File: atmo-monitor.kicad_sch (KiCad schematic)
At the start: 27 parts, among them J1 E-Ink, J2 Power, J3 Qwiic, J4 PM Sensor, SW1 Reset, SW2 1825232-1, U1 STM32F103CBT6, U2 LP2950-3.3_TO252

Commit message: Finished initial design
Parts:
- added Q1: IRLML0100TRPbF, Package_TO_SOT_SMD:SOT-23, symbol Transistor_FET:IRLML0030
- renumbered J2 to U3
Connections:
- net +3.3V: now also Q1.1 (G)
- net ENABLE: now also SW2.1 (B)
- net LBO: now also Q1.3 (D); no longer SW2.1 (B)
- net MCU-LBO: now reaches U1.10 (PA0)
- net MCU-LBO: now also Q1.2 (S)
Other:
- note added: "5V & Battery Power"
- note added: "Level Translation"
- moved on the sheet: H1, H2, H3, H4, J3, U3

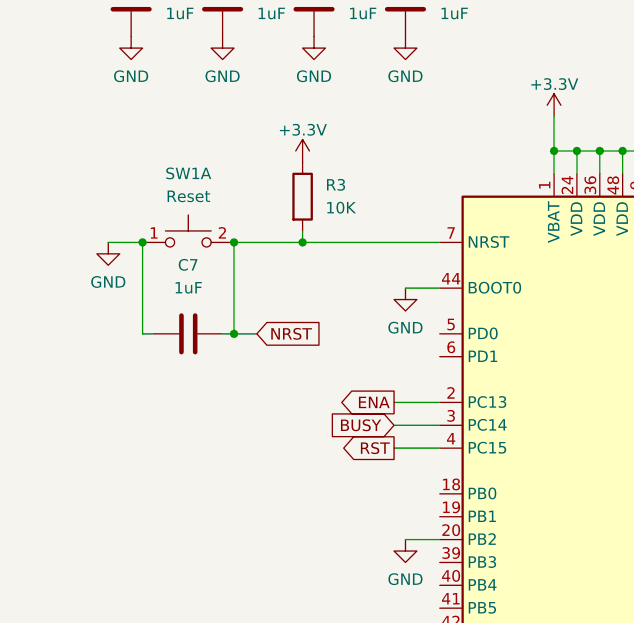
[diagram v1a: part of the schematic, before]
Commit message: Moved 2 signals from output limited ports
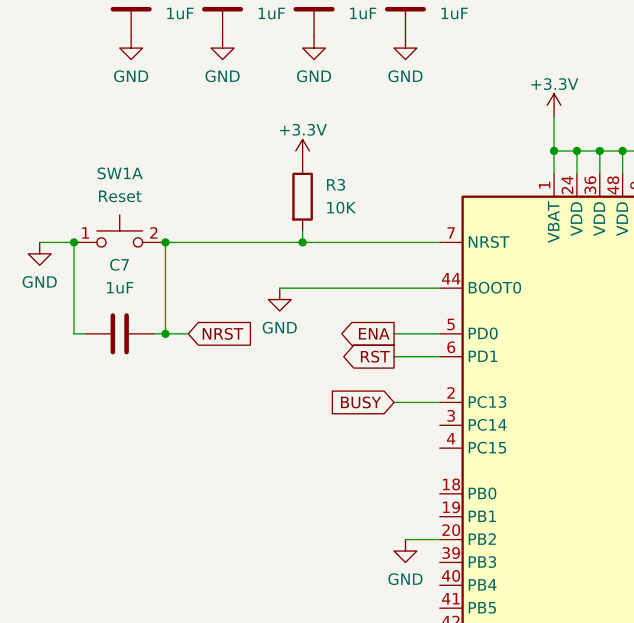
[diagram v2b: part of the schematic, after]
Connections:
- net BUSY: now also U1.2 (PC13); no longer U1.3 (PC14)
- net ENA: now also U1.5 (PD0); no longer U1.2 (PC13)
- net RST: now also U1.6 (PD1); no longer U1.4 (PC15)
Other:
- moved on the sheet: C7, SW1A
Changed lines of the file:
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@@
 	)
 	(junction
-		(at 45.72 57.15)
-		(diameter 0)
-		(color 0 0 0 0)
-	)
-	(junction
 		(at 204.47 30.48)
 		(diameter 0)
@@
 	)
 	(junction
-		(at 45.72 67.31)
+		(at 38.1 67.31)
 		(diameter 0)
 		(color 0 0 0 0)
@@
 	)
 	(junction
+		(at 38.1 57.15)
+		(diameter 0)
+		(color 0 0 0 0)
+	)
+	(junction
 		(at 165.1 50.8)
 		(diameter 0)
@@
 	)
 	(junction
-		(at 35.56 57.15)
+		(at 27.94 57.15)
 		(diameter 0)
 		(color 0 0 0 0)
@@
 	(wire
 		(pts
-			(xy 63.5 80.01) (xy 68.58 80.01)
+			(xy 63.5 69.85) (xy 68.58 69.85)
 		)
 		(stroke
@@
 	(wire
 		(pts
-			(xy 104.14 64.77) (xy 109.22 64.77)
+			(xy 38.1 57.15) (xy 53.34 57.15)
 		)
 		(stroke
@@
 	(wire
 		(pts
-			(xy 45.72 67.31) (xy 44.45 67.31)
+			(xy 104.14 64.77) (xy 109.22 64.77)
 		)
 		(stroke
@@
 	(wire
 		(pts
-			(xy 45.72 67.31) (xy 48.26 67.31)
+			(xy 38.1 67.31) (xy 36.83 67.31)
 		)
 		(stroke
@@
 	(wire
 		(pts
-			(xy 165.1 50.8) (xy 170.18 50.8)
+			(xy 38.1 67.31) (xy 40.64 67.31)
 		)
 		(stroke
@@
 	(wire
 		(pts
-			(xy 91.44 49.53) (xy 91.44 46.99)
+			(xy 165.1 50.8) (xy 170.18 50.8)
 		)
 		(stroke
@@
 	(wire
 		(pts
-			(xy 45.72 57.15) (xy 53.34 57.15)
+			(xy 91.44 49.53) (xy 91.44 46.99)
 		)
 		(stroke
@@
 	(wire
 		(pts
-			(xy 36.83 67.31) (xy 35.56 67.31)
+			(xy 29.21 67.31) (xy 27.94 67.31)
 		)
 		(stroke
@@
 	(wire
 		(pts
-			(xy 64.77 62.23) (xy 68.58 62.23)
+			(xy 176.53 39.37) (xy 176.53 41.91)
 		)
 		(stroke
@@
 	(wire
 		(pts
-			(xy 176.53 39.37) (xy 176.53 41.91)
+			(xy 171.45 101.6) (xy 179.07 101.6)
 		)
 		(stroke
@@
 	(wire
 		(pts
-			(xy 171.45 101.6) (xy 179.07 101.6)
+			(xy 173.99 34.29) (xy 173.99 36.83)
 		)
 		(stroke
@@
 	(wire
 		(pts
-			(xy 173.99 34.29) (xy 173.99 36.83)
+			(xy 119.38 177.8) (xy 110.49 177.8)
 		)
 		(stroke
@@
 	(wire
 		(pts
-			(xy 119.38 177.8) (xy 110.49 177.8)
+			(xy 173.99 36.83) (xy 176.53 36.83)
 		)
 		(stroke
@@
 	(wire
 		(pts
-			(xy 173.99 36.83) (xy 176.53 36.83)
+			(xy 50.8 62.23) (xy 68.58 62.23)
 		)
 		(stroke
@@
 	(wire
 		(pts
-			(xy 31.75 57.15) (xy 35.56 57.15)
+			(xy 24.13 57.15) (xy 27.94 57.15)
 		)
 		(stroke
@@
 	(wire
 		(pts
-			(xy 63.5 77.47) (xy 68.58 77.47)
+			(xy 63.5 67.31) (xy 68.58 67.31)
 		)
 		(stroke
@@
 	(wire
 		(pts
-			(xy 45.72 57.15) (xy 45.72 67.31)
+			(xy 38.1 57.15) (xy 38.1 67.31)
 		)
 		(stroke
@@
 	(wire
 		(pts
-			(xy 35.56 67.31) (xy 35.56 57.15)
+			(xy 27.94 67.31) (xy 27.94 57.15)
 		)
 		(stroke
@@
 	(global_label "RST"
 		(shape output)
-		(at 63.5 80.01 180)
+		(at 63.5 69.85 180)
 		(fields_autoplaced yes)
 		(effects
@@
 		)
 		(property "Intersheetrefs" "${INTERSHEET_REFS}"
-			(at 57.0677 80.01 0)
+			(at 57.0677 69.85 0)
 			(effects
 				(font
@@
 	(global_label "NRST"
 		(shape input)
-		(at 48.26 67.31 0)
+		(at 40.64 67.31 0)
 		(fields_autoplaced yes)
 		(effects
@@
 		)
 		(property "Intersheetrefs" "${INTERSHEET_REFS}"
-			(at 56.0228 67.31 0)
+			(at 48.4028 67.31 0)
 			(effects
 				(font
@@
 	(global_label "BUSY"
 		(shape input)
-		(at 63.5 77.47 180)
+		(at 63.5 74.93 180)
 		(fields_autoplaced yes)
 		(effects
@@
 		)
 		(property "Intersheetrefs" "${INTERSHEET_REFS}"
-			(at 55.6162 77.47 0)
+			(at 55.6162 74.93 0)
 			(effects
 				(font
@@
 	(global_label "ENA"
 		(shape output)
-		(at 63.5 74.93 180)
+		(at 63.5 67.31 180)
 		(fields_autoplaced yes)
 		(effects
@@
 		)
 		(property "Intersheetrefs" "${INTERSHEET_REFS}"
-			(at 56.9467 74.93 0)
+			(at 56.9467 67.31 0)
 			(effects
 				(font
@@
 	(symbol
 		(lib_id "Device:C")
-		(at 40.64 67.31 270)
+		(at 33.02 67.31 270)
 		(unit 1)
 		(exclude_from_sim no)
@@
 		(fields_autoplaced yes)
 		(property "Reference" "C7"
-			(at 40.64 59.69 90)
+			(at 33.02 59.69 90)
 			(effects
 				(font
@@
 		)
 		(property "Value" "1uF"
-			(at 40.64 62.23 90)
+			(at 33.02 62.23 90)
 			(effects
 				(font
@@
 		)
 		(property "Footprint" "Capacitor_SMD:C_1206_3216Metric_Pad1.33x1.80mm_HandSolder"
-			(at 36.83 68.2752 0)
+			(at 29.21 68.2752 0)
 			(effects
 				(font
@@
 		)
 		(property "Datasheet" "~"
-			(at 40.64 67.31 0)
+			(at 33.02 67.31 0)
 			(effects
 				(font
@@
 		)
 		(property "Description" "Unpolarized capacitor"
-			(at 40.64 67.31 0)
+			(at 33.02 67.31 0)
 			(effects
 				(font
@@
 	(symbol
 		(lib_id "Switch:SW_Push_Dual_x2")
-		(at 40.64 57.15 0)
+		(at 33.02 57.15 0)
 		(unit 1)
 		(exclude_from_sim no)
@@
 		(fields_autoplaced yes)
 		(property "Reference" "SW1"
-			(at 40.64 49.53 0)
+			(at 33.02 49.53 0)
 			(effects
 				(font
@@
 		)
 		(property "Value" "Reset"
-			(at 40.64 52.07 0)
+			(at 33.02 52.07 0)
 			(effects
 				(font
@@
 		)
 		(property "Footprint" "custom_footprint:OnShine KPT-1187B"
-			(at 40.64 52.07 0)
+			(at 33.02 52.07 0)
 			(effects
 				(font
@@
 		)
 		(property "Datasheet" "~"
-			(at 40.64 52.07 0)
+			(at 33.02 52.07 0)
 			(effects
 				(font
@@
 		)
 		(property "Description" "Push button switch, generic, separate symbols, four pins"
-			(at 40.64 57.15 0)
+			(at 33.02 57.15 0)
 			(effects
 				(font
@@
 	(symbol
 		(lib_id "power:GND")
-		(at 64.77 62.23 0)
+		(at 50.8 62.23 0)
 		(unit 1)
 		(exclude_from_sim no)
@@
 		(fields_autoplaced yes)
 		(property "Reference" "#PWR021"
-			(at 64.77 68.58 0)
+			(at 50.8 68.58 0)
 			(effects
 				(font
@@
 		)
 		(property "Value" "GND"
-			(at 64.77 66.6734 0)
+			(at 50.8 66.6734 0)
 			(effects
 				(font
@@
 		)
 		(property "Footprint" ""
-			(at 64.77 62.23 0)
+			(at 50.8 62.23 0)
 			(effects
 				(font
@@
 		)
 		(property "Datasheet" ""
-			(at 64.77 62.23 0)
+			(at 50.8 62.23 0)
 			(effects
 				(font
@@
 		)
 		(property "Description" ""
-			(at 64.77 62.23 0)
+			(at 50.8 62.23 0)
 			(effects
 				(font
@@
 	(symbol
 		(lib_id "power:GND")
-		(at 31.75 57.15 0)
+		(at 24.13 57.15 0)
 		(unit 1)
 		(exclude_from_sim no)
@@
 		(fields_autoplaced yes)
 		(property "Reference" "#PWR022"
-			(at 31.75 63.5 0)
+			(at 24.13 63.5 0)
 			(effects
 				(font
@@
 		)
 		(property "Value" "GND"
-			(at 31.75 61.5934 0)
+			(at 24.13 61.5934 0)
 			(effects
 				(font
@@
 		)
 		(property "Footprint" ""
-			(at 31.75 57.15 0)
+			(at 24.13 57.15 0)
 			(effects
 				(font
@@
 		)
 		(property "Datasheet" ""
-			(at 31.75 57.15 0)
+			(at 24.13 57.15 0)
 			(effects
 				(font
@@
 		)
 		(property "Description" ""
-			(at 31.75 57.15 0)
+			(at 24.13 57.15 0)
 			(effects
 				(font

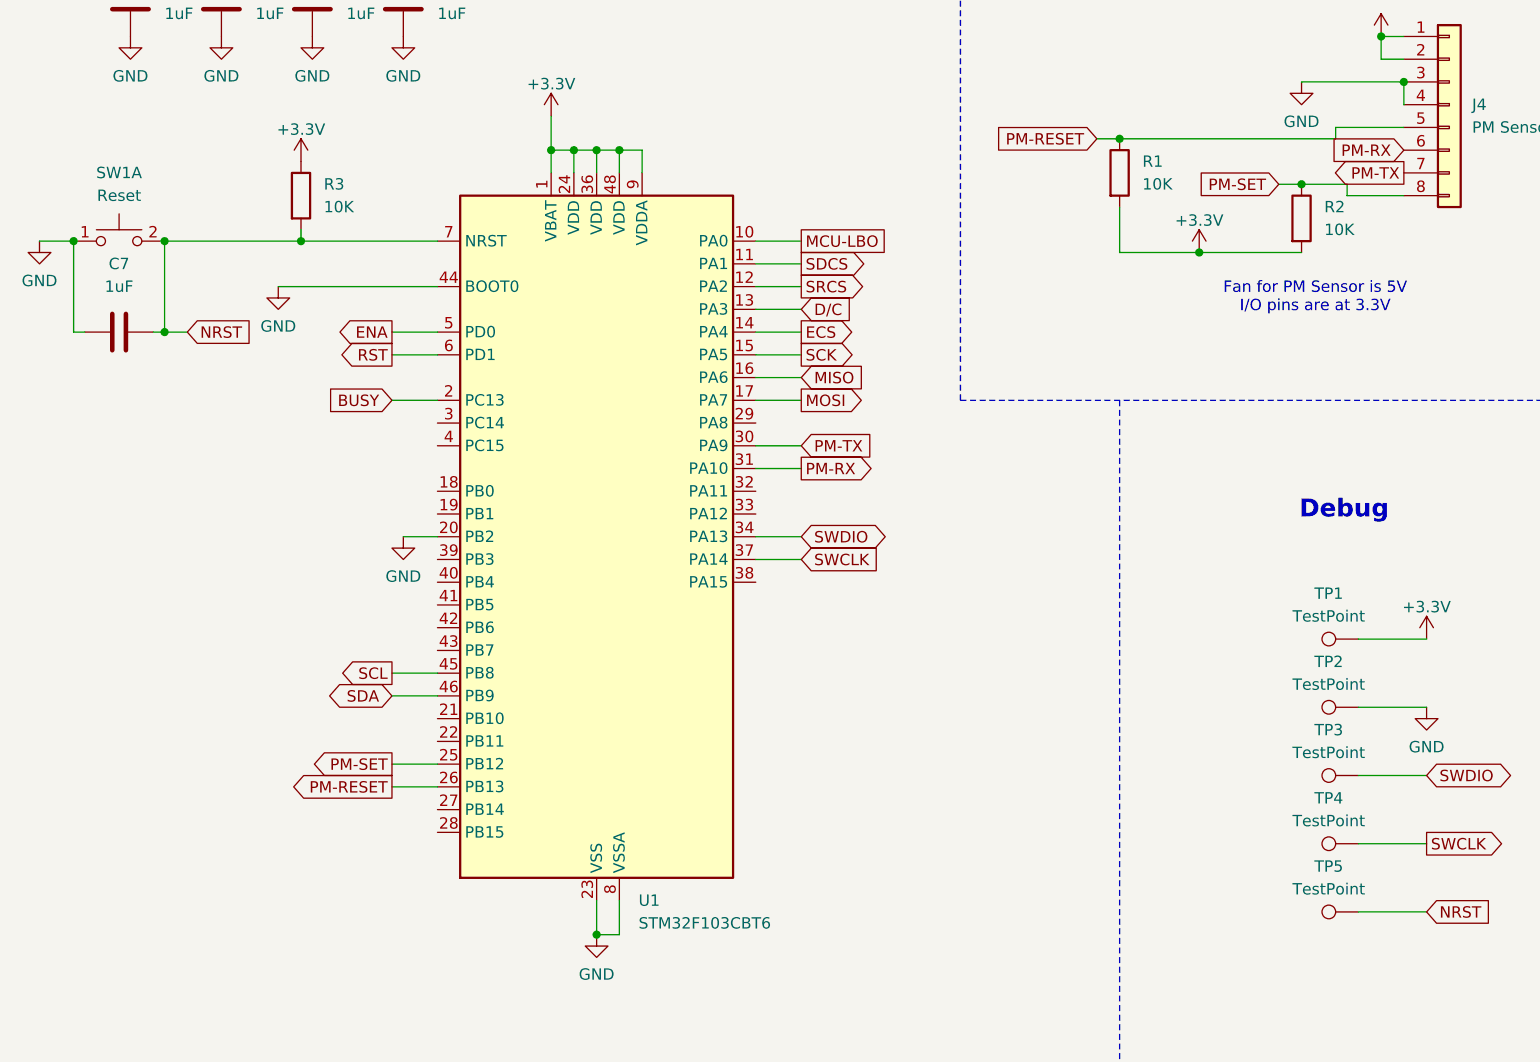
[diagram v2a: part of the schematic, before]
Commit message: Added R4 for SWCLK
Reordered debug test points
Fixed schematic DRC problems
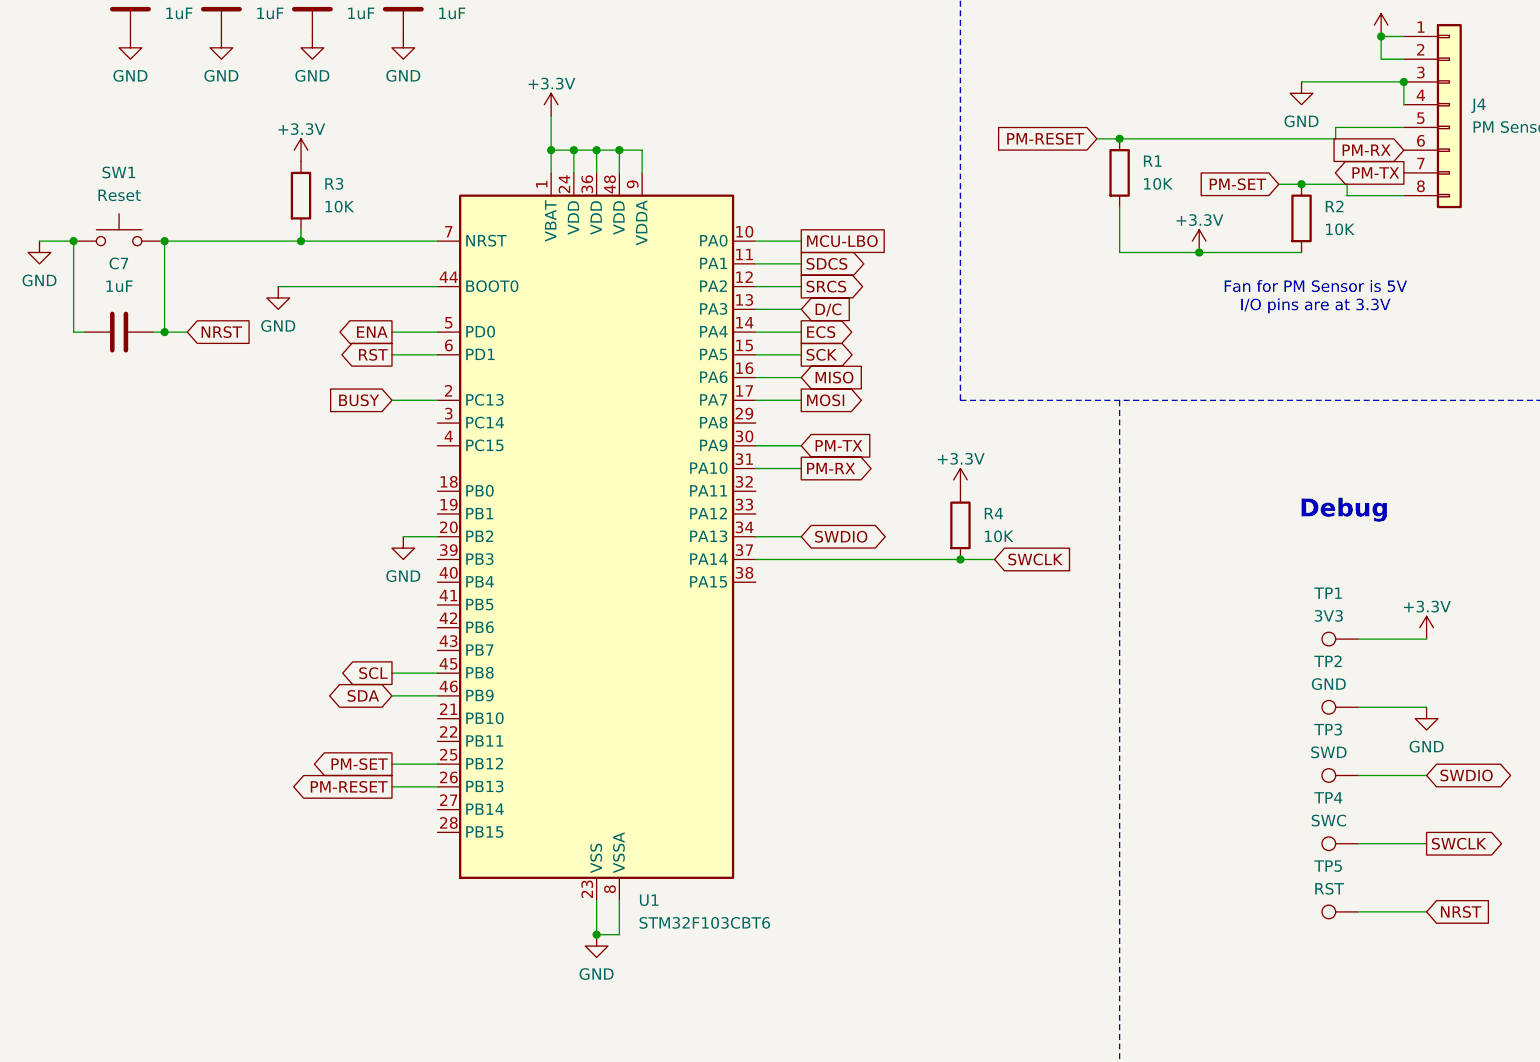
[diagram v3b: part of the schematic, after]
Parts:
- removed SW1: Reset, custom_footprint:OnShine KPT-1187B, symbol Switch:SW_Push_Dual_x2
- added R4: 10K, Resistor_SMD:R_1206_3216Metric_Pad1.30x1.75mm_HandSolder, symbol Device:R
- added SW1: Reset, symbol Switch:SW_Push
- TP1: value TestPoint -> 3V3
- TP2: value TestPoint -> GND
- TP3: value TestPoint -> SWD
- TP4: value TestPoint -> SWC
- TP5: value TestPoint -> RST
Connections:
- net +3.3V: now also R4.1
- net GND: now also SW1.1
- net NRST: now also SW1.2
- net SWCLK: now also R4.2
